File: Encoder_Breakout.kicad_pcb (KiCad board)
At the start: 2 copper layers, 35.6 x 33.7 mm, 4 parts, among them J1 5-104363-1, J2 Conn_02x07_Odd_Even, J5 5-104935-3, J6 5-104363-1

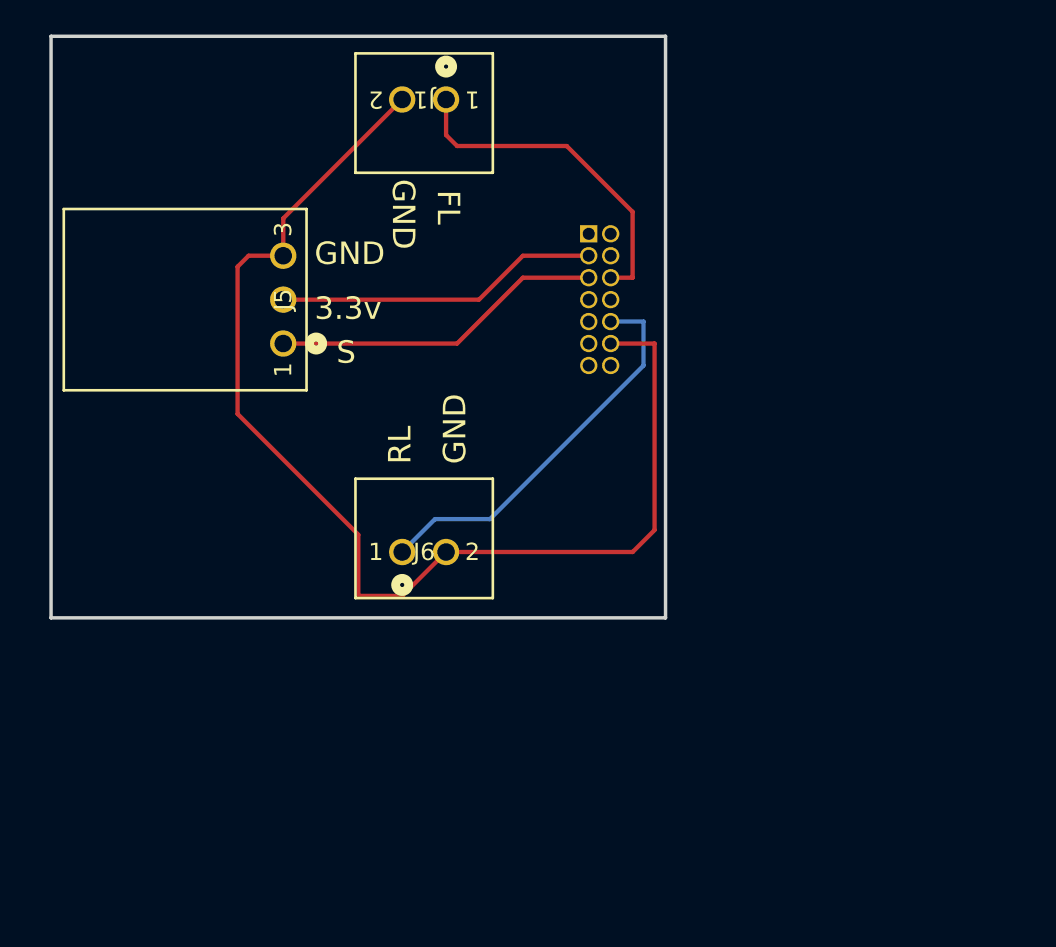
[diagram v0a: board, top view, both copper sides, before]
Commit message: Reshape to sparkmax and add LEDs
Signed-off-by: Colin <cfinn68916@gmail.com>
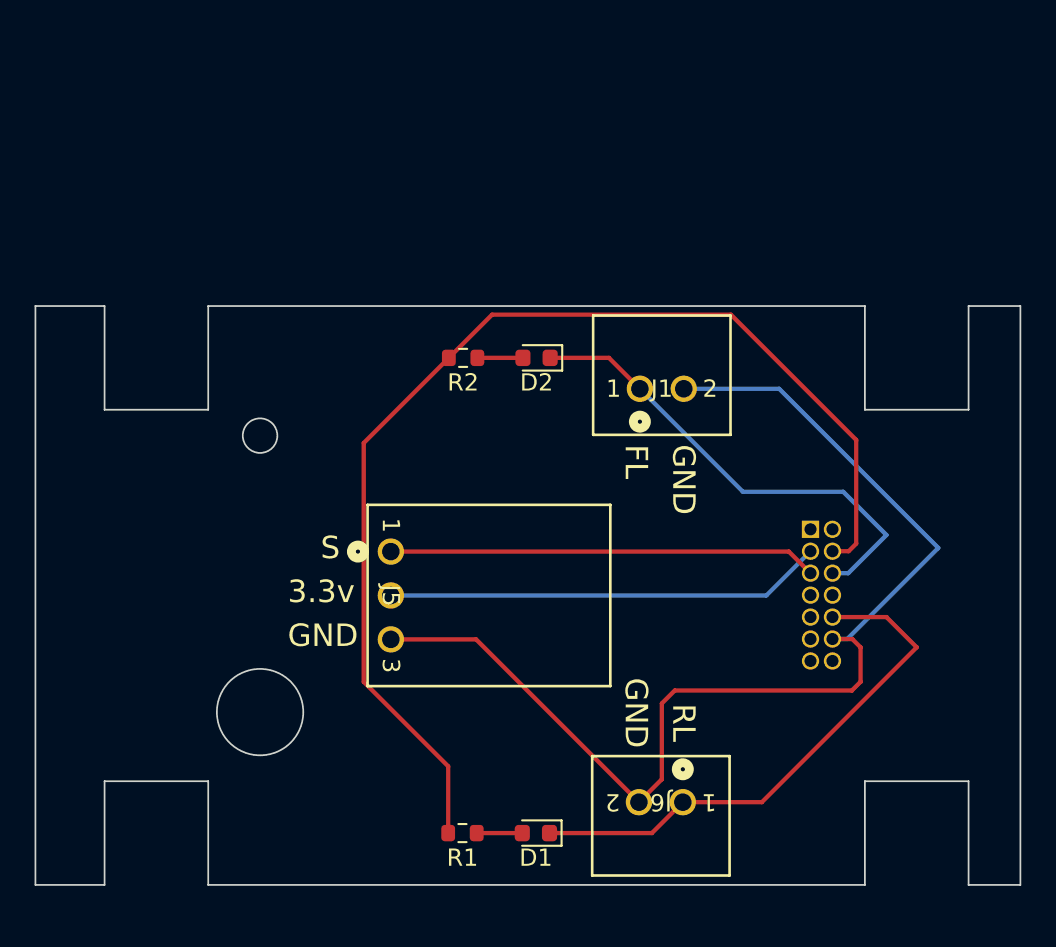
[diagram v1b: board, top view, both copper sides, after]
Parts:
- added D1: LED, LED_SMD:LED_0603_1608Metric, F.Cu at (157.0, 118.5)
- added D2: LED, LED_SMD:LED_0603_1608Metric, F.Cu at (157.0, 91.0)
- added R1: 270Ω, Resistor_SMD:R_0603_1608Metric, F.Cu at (152.7, 118.5)
- added R2: 270Ω, Resistor_SMD:R_0603_1608Metric, F.Cu at (152.8, 91.0)
- moved J6 21.8 mm to (165.5, 116.7), turned to 180 degrees
- moved J2 21.4 mm to (172.9, 100.9)
- moved J1 20.1 mm to (163.0, 92.8), turned to 0 degrees
- moved J5 13.6 mm to (148.6, 102.2), turned to -90 degrees
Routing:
- net +5V: track 0.00 -> 66.7 mm
- net Net-(D1-K): track 22.9 -> 31.3 mm
- net Net-(D2-K): track 19.8 -> 27.7 mm
- net +3.3V: track 18.7 -> 25.3 mm
- net Net-(J2-Pin_5): track 19.3 -> 24.8 mm
- net Net-(D2-A): track 0.00 -> 2.64 mm
- net Net-(D1-A): track 0.00 -> 2.64 mm
- net GND: track 68.8 -> 67.2 mm
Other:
- board size 35.6 x 33.7 mm -> 57 x 33.5 mm
- board text removed: "SPARKMAX ThriftyBot Encoder Breakout Board"
- board text removed: "V1"

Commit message: Add text where it is covered on SPARKMAX
Signed-off-by: Colin <cfinn68916@gmail.com>
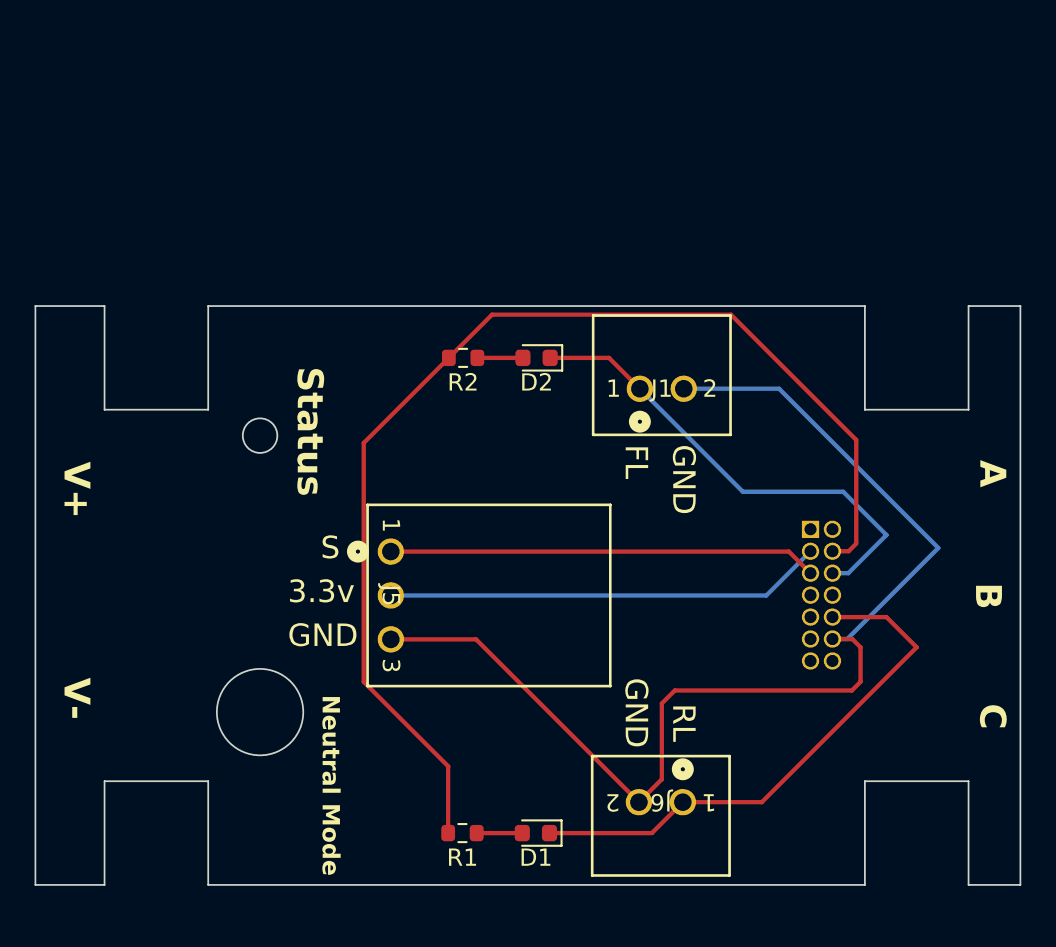
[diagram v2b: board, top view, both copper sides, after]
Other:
- board text added: "A"
- board text added: "B"
- board text added: "C"
- board text added: "Neutral Mode"
- board text added: "Status"
- board text added: "V+"
- board text added: "V-"
- board text removed: "C. Finn"
- board text removed: "FRC Team 1716 Redbird Robotics"
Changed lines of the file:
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@@
   (gr_circle (center 141 111.5) (end 138.5 111.5)
     (stroke (width 0.1) (type default)) (fill none) (layer "Edge.Cuts"))
-  (gr_text "FRC Team 1716\nRedbird Robotics" (at 111.25 40.75) (layer "B.SilkS")
-    (effects (font (size 1.5 1.5) (thickness 0.3) bold) (justify left bottom mirror))
-  )
-  (gr_text "C. Finn" (at 137.795 60.96) (layer "B.SilkS")
-    (effects (font (size 1.5 1.5) (thickness 0.3) bold) (justify left bottom mirror))
+  (gr_text "V-" (at 129.5 109.5 -90) (layer "F.SilkS")
+    (effects (font (size 1.5 1.5) (thickness 0.3) bold) (justify left bottom))
   )
   (gr_text "S" (at 144.5 102.75) (layer "F.SilkS")
     (effects (font (size 1.3 1.3) (thickness 0.2)) (justify left bottom))
   )
+  (gr_text "Neutral Mode" (at 144.5 110.5 270) (layer "F.SilkS")
+    (effects (font (size 1 1) (thickness 0.17) bold) (justify left bottom))
+  )
   (gr_text "RL" (at 164.75 111 -90) (layer "F.SilkS")
     (effects (font (size 1.3 1.3) (thickness 0.2)) (justify left bottom))
+  )
+  (gr_text "Status" (at 143 91.5 270) (layer "F.SilkS")
+    (effects (font (size 1.5 1.5) (thickness 0.3) bold) (justify left bottom))
   )
   (gr_text "GND" (at 162 109.5 -90) (layer "F.SilkS")
     (effects (font (size 1.3 1.3) (thickness 0.2)) (justify left bottom))
   )
+  (gr_text "C" (at 182.5 111 -90) (layer "F.SilkS")
+    (effects (font (size 1.5 1.5) (thickness 0.3) bold) (justify left bottom))
+  )
+  (gr_text "B" (at 182.25 104 -90) (layer "F.SilkS")
+    (effects (font (size 1.5 1.5) (thickness 0.3) bold) (justify left bottom))
+  )
   (gr_text "GND" (at 164.75 96 270) (layer "F.SilkS")
     (effects (font (size 1.3 1.3) (thickness 0.2)) (justify left bottom))
   )
+  (gr_text "V+" (at 129.5 97 -90) (layer "F.SilkS")
+    (effects (font (size 1.5 1.5) (thickness 0.3) bold) (justify left bottom))
+  )
+  (gr_text "A" (at 182.5 98.5 -90) (layer "F.SilkS")
+    (effects (font (size 1.5 1.5) (thickness 0.3) bold) (justify left bottom mirror))
+  )
   (gr_text "3.3v" (at 142.595 105.29) (layer "F.SilkS")

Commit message: Add metadata to backside
Signed-off-by: Colin <cfinn68916@gmail.com>
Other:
- board text added: "Batch 0"
- board text added: "C. Finn"
- board text added: "Cover me with a ziptie!"
- board text added: "SPARKMAX Breakout Board V2 FRC 1716 Redbird Robotics"
- board text added: "https://github.com/Brown-County-FIRST-Robotics/SPARKMAX_Breakout"
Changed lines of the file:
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@@
   (gr_circle (center 141 111.5) (end 138.5 111.5)
     (stroke (width 0.1) (type default)) (fill none) (layer "Edge.Cuts"))
+  (gr_text "Cover me with a ziptie!" (at 134 94.5 270) (layer "F.Cu")
+    (effects (font (size 1.1 1.1) (thickness 0.25) bold) (justify left bottom))
+  )
+  (gr_text "SPARKMAX Breakout\nBoard V2\n\nFRC 1716\nRedbird Robotics" (at 160 104.5 270) (layer "B.SilkS")
+    (effects (font (size 1.5 1.5) (thickness 0.3) bold) (justify bottom mirror))
+  )
+  (gr_text "https://github.com/Brown-County-FIRST-Robotics/SPARKMAX_Breakout" (at 129.5 120.5 270) (layer "B.SilkS")
+    (effects (font (size 0.57 0.57) (thickness 0.1) bold) (justify left bottom mirror))
+  )
+  (gr_text "Batch 0" (at 147.5 121) (layer "B.SilkS")
+    (effects (font (size 1.5 1.5) (thickness 0.3) bold) (justify left bottom mirror))
+  )
+  (gr_text "C. Finn" (at 146.5 90.5) (layer "B.SilkS")
+    (effects (font (size 1.5 1.5) (thickness 0.3) bold) (justify left bottom mirror))
+  )
   (gr_text "V-" (at 129.5 109.5 -90) (layer "F.SilkS")
     (effects (font (size 1.5 1.5) (thickness 0.3) bold) (justify left bottom))
